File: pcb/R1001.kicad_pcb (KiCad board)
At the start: 4 copper layers, 51 x 33.3 mm, 50 parts, among them J1 PCIEXPRESS-X1, J2 CONN_01X04, Q1 Q_NMOS_GSD, U1 DRV8825, U2 74LS157, U3 EFM8BB10F8G, U4 ZXCT1107

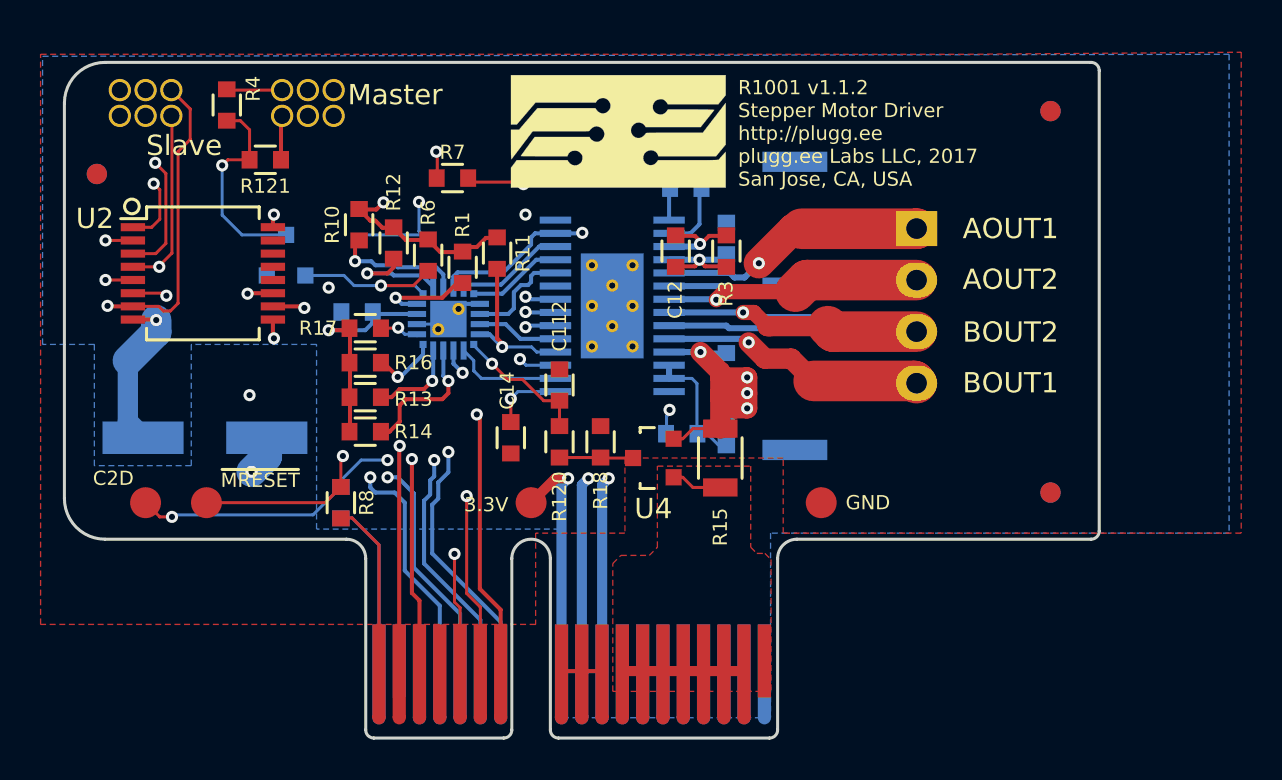
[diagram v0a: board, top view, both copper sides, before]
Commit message: fixed PCB outline for DFM, more space for bonding connectors
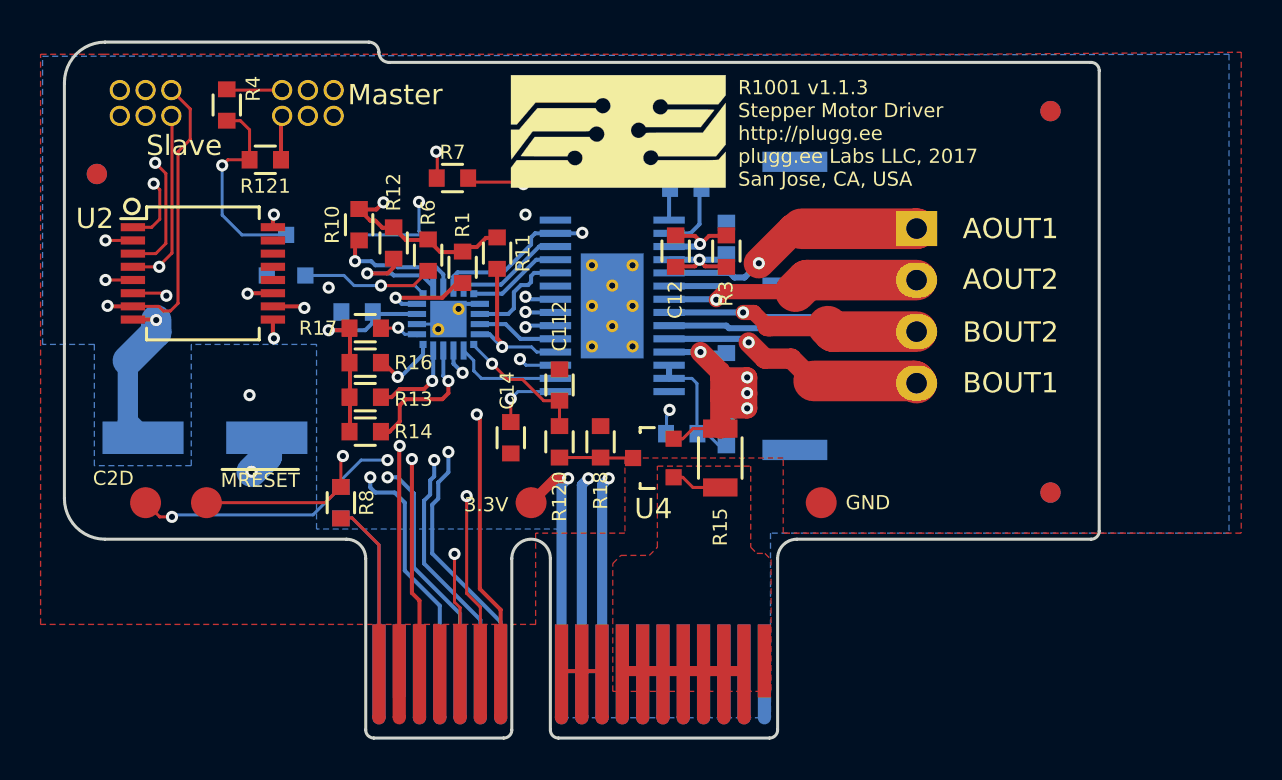
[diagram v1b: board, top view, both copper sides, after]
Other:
- board size 51 x 33.3 mm -> 51 x 34.3 mm
- board text added: "R1001 v1.1.3 Stepper Motor Driver http://plugg.ee plugg.ee Labs LLC, 2017 San Jose, CA, USA"
- board text removed: "R1001 v1.1.2 Stepper Motor Driver http://plugg.ee plugg.ee Labs LLC, 2017 San Jose, CA, USA"
